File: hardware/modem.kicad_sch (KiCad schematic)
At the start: 30 parts, among them J11 Conn_01x02, Q3 PMOS, Q4 Q_NPN_BEC, U6 SN74AVC4T245PW, U7 SARA-R500S-61B

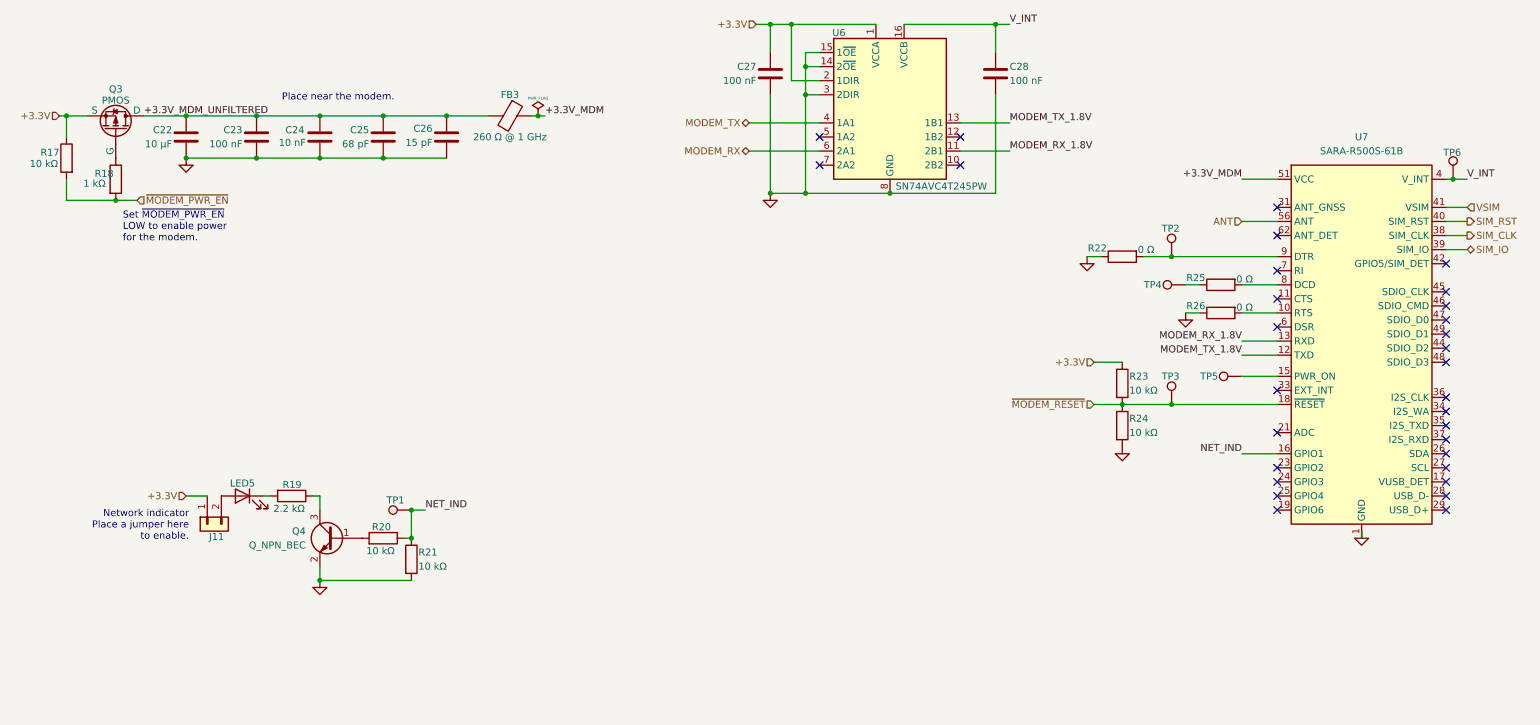
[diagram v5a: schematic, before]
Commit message: HW: Add series termination to UART lines
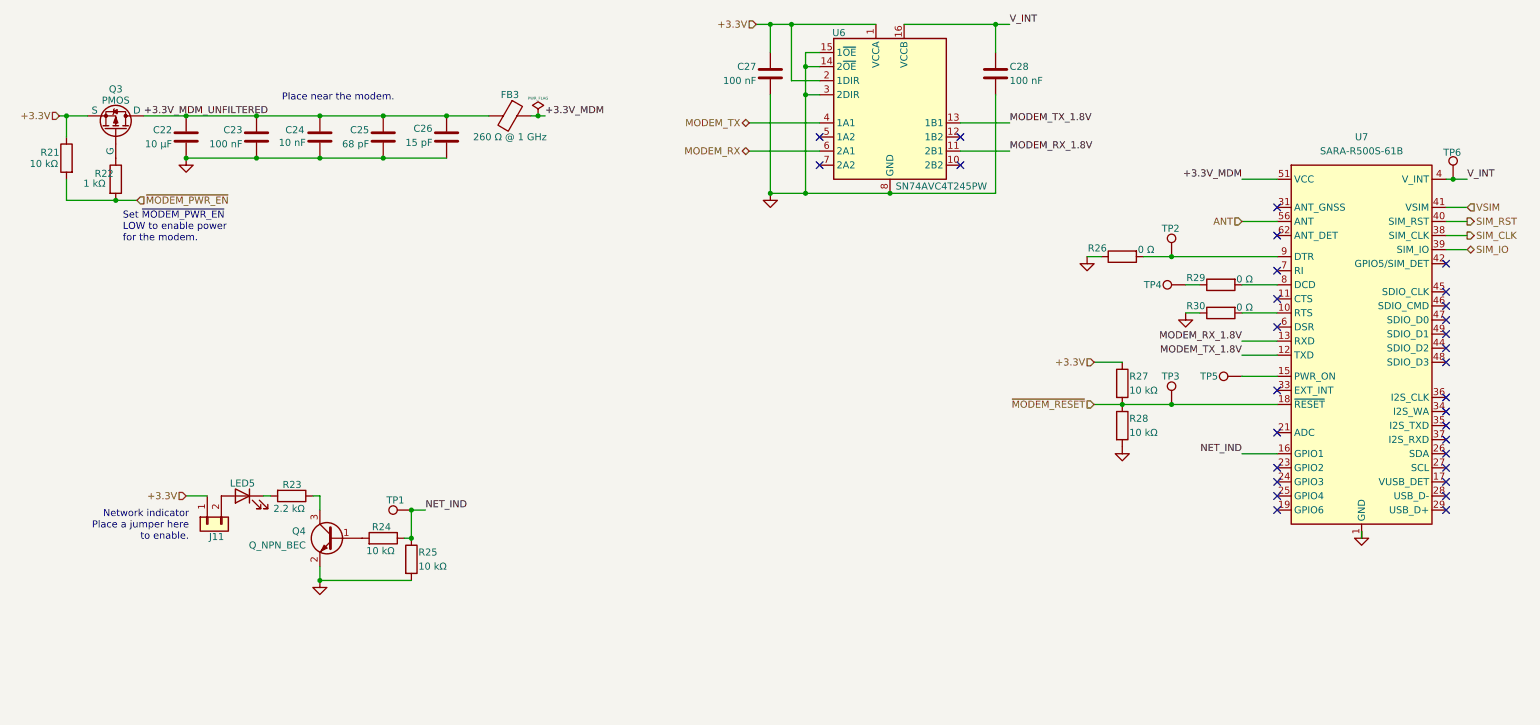
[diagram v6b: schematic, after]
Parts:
- renumbered R17 to R21, R18 to R22, R19 to R23, R20 to R24, R21 to R25, R22 to R26, R23 to R27, R24 to R28, R25 to R29, R26 to R30
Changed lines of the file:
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@@
 		(on_board yes)
 		(dnp no)
-		(property "Reference" "R23"
+		(property "Reference" "R27"
 			(at 213.36 134.62 0)
 			(effects
@@
 			(project "iida_devkit"
 				(path "/b12a6e25-97fb-4aba-bc96-af8db389bb9a/3723475b-e956-4027-ac40-e47346743900"
-					(reference "R23")
+					(reference "R27")
 					(unit 1)
 				)
@@
 		(on_board yes)
 		(dnp no)
-		(property "Reference" "R20"
+		(property "Reference" "R24"
 			(at 76.708 161.798 90)
 			(effects
@@
 			(project "iida_devkit"
 				(path "/b12a6e25-97fb-4aba-bc96-af8db389bb9a/3723475b-e956-4027-ac40-e47346743900"
-					(reference "R20")
+					(reference "R24")
 					(unit 1)
 				)
@@
 		(on_board yes)
 		(dnp no)
-		(property "Reference" "R24"
+		(property "Reference" "R28"
 			(at 213.36 142.24 0)
 			(effects
@@
 			(project "iida_devkit"
 				(path "/b12a6e25-97fb-4aba-bc96-af8db389bb9a/3723475b-e956-4027-ac40-e47346743900"
-					(reference "R24")
+					(reference "R28")
 					(unit 1)
 				)
@@
 		(on_board yes)
 		(dnp no)
-		(property "Reference" "R21"
+		(property "Reference" "R25"
 			(at 85.09 166.37 0)
 			(effects
@@
 			(project "iida_devkit"
 				(path "/b12a6e25-97fb-4aba-bc96-af8db389bb9a/3723475b-e956-4027-ac40-e47346743900"
-					(reference "R21")
+					(reference "R25")
 					(unit 1)
 				)
@@
 		(on_board yes)
 		(dnp no)
-		(property "Reference" "R17"
+		(property "Reference" "R21"
 			(at 20.32 94.234 0)
 			(effects
@@
 			(project "iida_devkit"
 				(path "/b12a6e25-97fb-4aba-bc96-af8db389bb9a/3723475b-e956-4027-ac40-e47346743900"
-					(reference "R17")
+					(reference "R21")
 					(unit 1)
 				)
@@
 		(on_board yes)
 		(dnp no)
-		(property "Reference" "R18"
+		(property "Reference" "R22"
 			(at 26.67 98.044 0)
 			(effects
@@
 			(project "iida_devkit"
 				(path "/b12a6e25-97fb-4aba-bc96-af8db389bb9a/3723475b-e956-4027-ac40-e47346743900"
-					(reference "R18")
+					(reference "R22")
 					(unit 1)
 				)
@@
 		(on_board yes)
 		(dnp no)
-		(property "Reference" "R26"
+		(property "Reference" "R30"
 			(at 227.076 121.92 90)
 			(effects
@@
 			(project "iida_devkit"
 				(path "/b12a6e25-97fb-4aba-bc96-af8db389bb9a/3723475b-e956-4027-ac40-e47346743900"
-					(reference "R26")
+					(reference "R30")
 					(unit 1)
 				)
@@
 		(on_board yes)
 		(dnp no)
-		(property "Reference" "R19"
+		(property "Reference" "R23"
 			(at 64.008 154.178 90)
 			(effects
@@
 			(project "iida_devkit"
 				(path "/b12a6e25-97fb-4aba-bc96-af8db389bb9a/3723475b-e956-4027-ac40-e47346743900"
-					(reference "R19")
+					(reference "R23")
 					(unit 1)
 				)
@@
 		(on_board yes)
 		(dnp no)
-		(property "Reference" "R22"
+		(property "Reference" "R26"
 			(at 209.296 111.506 90)
 			(effects
@@
 			(project "iida_devkit"
 				(path "/b12a6e25-97fb-4aba-bc96-af8db389bb9a/3723475b-e956-4027-ac40-e47346743900"
-					(reference "R22")
+					(reference "R26")
 					(unit 1)
 				)
@@
 		(on_board yes)
 		(dnp no)
-		(property "Reference" "R25"
+		(property "Reference" "R29"
 			(at 227.076 116.84 90)
 			(effects
@@
 			(project "iida_devkit"
 				(path "/b12a6e25-97fb-4aba-bc96-af8db389bb9a/3723475b-e956-4027-ac40-e47346743900"
-					(reference "R25")
+					(reference "R29")
 					(unit 1)
 				)

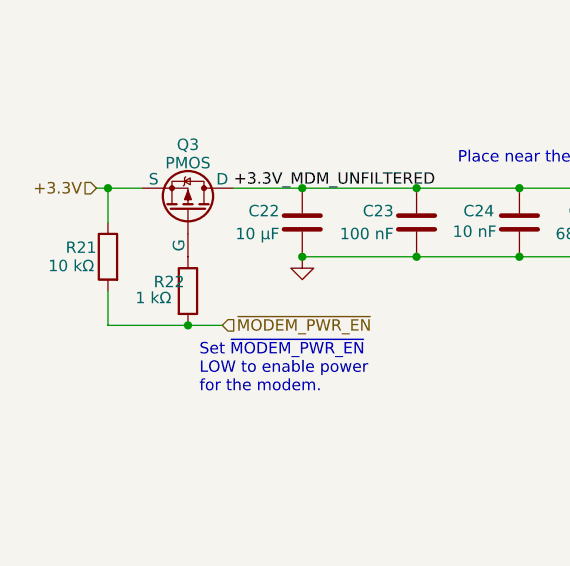
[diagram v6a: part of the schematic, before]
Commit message: HW: Layout Modem and SIM
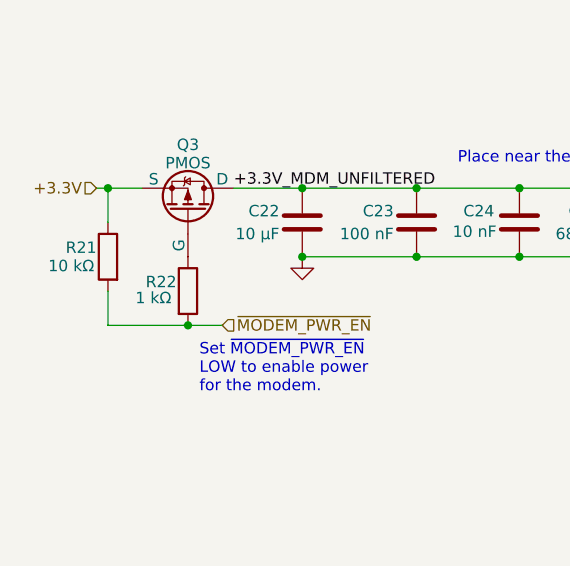
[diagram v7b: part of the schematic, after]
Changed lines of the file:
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@@
 		(dnp no)
 		(property "Reference" "R22"
-			(at 26.67 98.044 0)
+			(at 29.21 98.044 0)
 			(effects
 				(font
 					(size 1.27 1.27)
 				)
-				(justify left)
+				(justify right)
 			)
 		)

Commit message: HW: Finish layout
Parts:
- TP1, TP2, TP3, TP4, TP6: now left out of the parts list
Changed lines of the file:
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@@
 	(title_block
 		(title "Iida devkit")
-		(date "2024-09-10")
-		(rev "v4.0.0")
+		(date "2024-09-21")
+		(rev "v4.1.0")
 	)
 	(junction
@@
 		(unit 1)
 		(exclude_from_sim no)
-		(in_bom yes)
+		(in_bom no)
 		(on_board yes)
 		(dnp no)
@@
 		(unit 1)
 		(exclude_from_sim no)
-		(in_bom yes)
+		(in_bom no)
 		(on_board yes)
 		(dnp no)
@@
 		(unit 1)
 		(exclude_from_sim no)
-		(in_bom yes)
+		(in_bom no)
 		(on_board yes)
 		(dnp no)
@@
 		(unit 1)
 		(exclude_from_sim no)
-		(in_bom yes)
+		(in_bom no)
 		(on_board yes)
 		(dnp no)
@@
 		(unit 1)
 		(exclude_from_sim no)
-		(in_bom yes)
+		(in_bom no)
 		(on_board yes)
 		(dnp no)
